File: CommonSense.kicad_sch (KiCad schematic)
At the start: 37 parts, among them J1 Conn_02x04_Counter_Clockwise, J2 Conn_01x02, J3 Conn_01x02, J5 Conn_ARM_SWD_TagConnect_TC203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, U1 NRF52810-QFAA-R7, U2 SHT41-AD1B-R2, Y1 ECS-.327-12.5-12R-TR, Y2 ABM11W-32.0000MHZ-7-D1X-T3

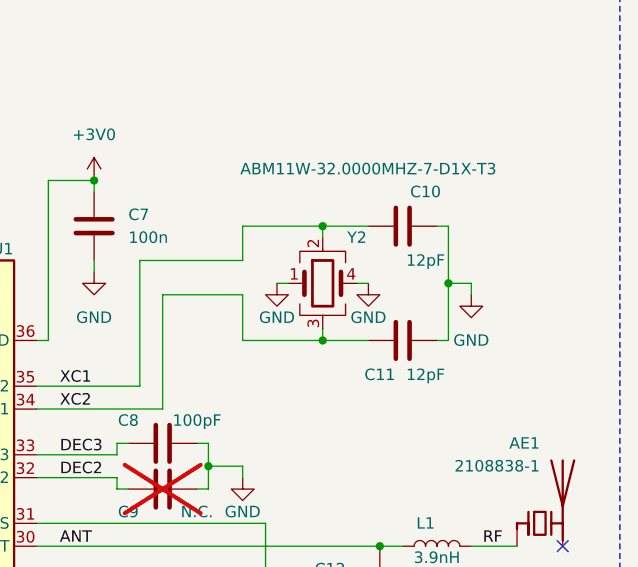
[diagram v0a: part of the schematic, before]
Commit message: Change crystal capacitor values
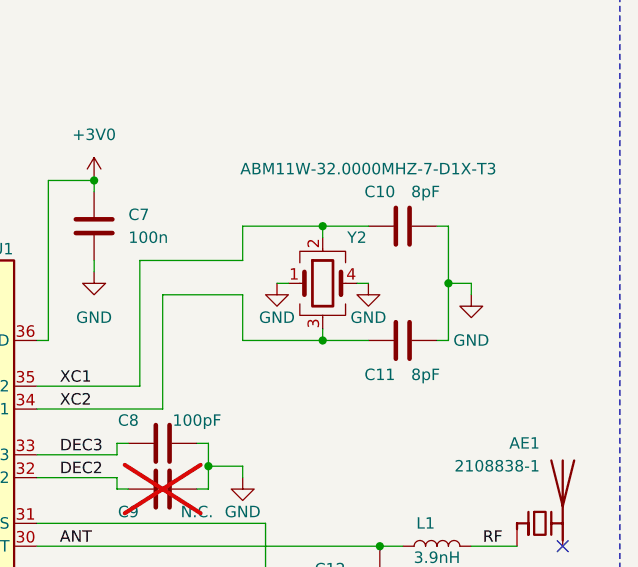
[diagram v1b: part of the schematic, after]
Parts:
- C10, C11: value 12pF -> 8pF
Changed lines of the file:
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@@
   (symbol (lib_id "Device:C") (at 251.46 66.04 90) (unit 1)
     (in_bom yes) (on_board yes) (dnp no)
-    (property "Reference" "C10" (at 254 62.23 90)
-      (effects (font (size 1.27 1.27)))
-    )
-    (property "Value" "12pF" (at 254 69.85 90)
+    (property "Reference" "C10" (at 248.92 62.23 90)
+      (effects (font (size 1.27 1.27)))
+    )
+    (property "Value" "8pF" (at 254 62.23 90)
       (effects (font (size 1.27 1.27)))
     )
@@
       (effects (font (size 1.27 1.27)))
     )
-    (property "Value" "12pF" (at 254 82.55 90)
-      (effects (font (size 1.27 1.27)))
-    )
+    (property "Value" "8pF" (at 254 82.55 90)
+      (effects (font (size 1.27 1.27)))
+    )

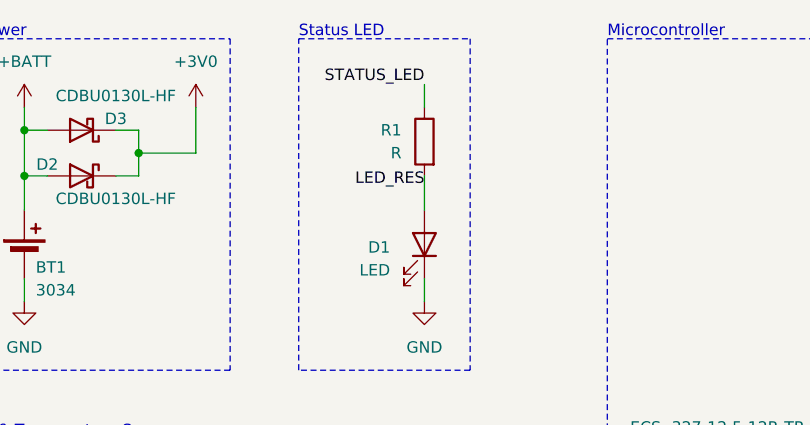
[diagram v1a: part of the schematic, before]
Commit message: Add 1k value to LED resistor
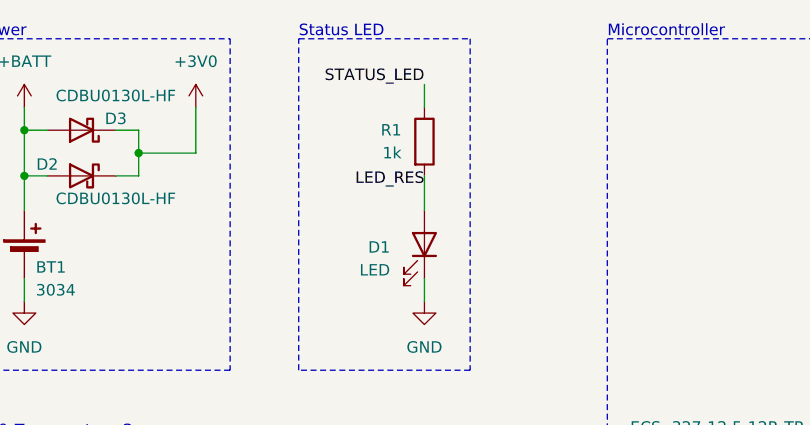
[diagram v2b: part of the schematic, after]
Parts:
- R1: value R -> 1k
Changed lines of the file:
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@@
     )
   )
-  (symbol (lib_id "Device:R") (at 72.39 44.45 0) (mirror y) (unit 1)
-    (in_bom yes) (on_board yes) (dnp no) (fields_autoplaced)
+  (symbol (lib_id "Device:R") (at 72.39 44.45 0) (unit 1)
+    (in_bom yes) (on_board yes) (dnp no)
     (property "Reference" "R1" (at 69.85 43.18 0)
-      (effects (font (size 1.27 1.27)) (justify left))
+      (effects (font (size 1.27 1.27)) (justify right))
     )
-    (property "Value" "R" (at 69.85 45.72 0)
-      (effects (font (size 1.27 1.27)) (justify left))
+    (property "Value" "1k" (at 69.85 45.72 0)
+      (effects (font (size 1.27 1.27)) (justify right))
     )
-    (property "Footprint" "Resistor_SMD:R_0603_1608Metric" (at 74.168 44.45 90)
+    (property "Footprint" "Resistor_SMD:R_0603_1608Metric" (at 70.612 44.45 90)
       (effects (font (size 1.27 1.27)) hide)
     )

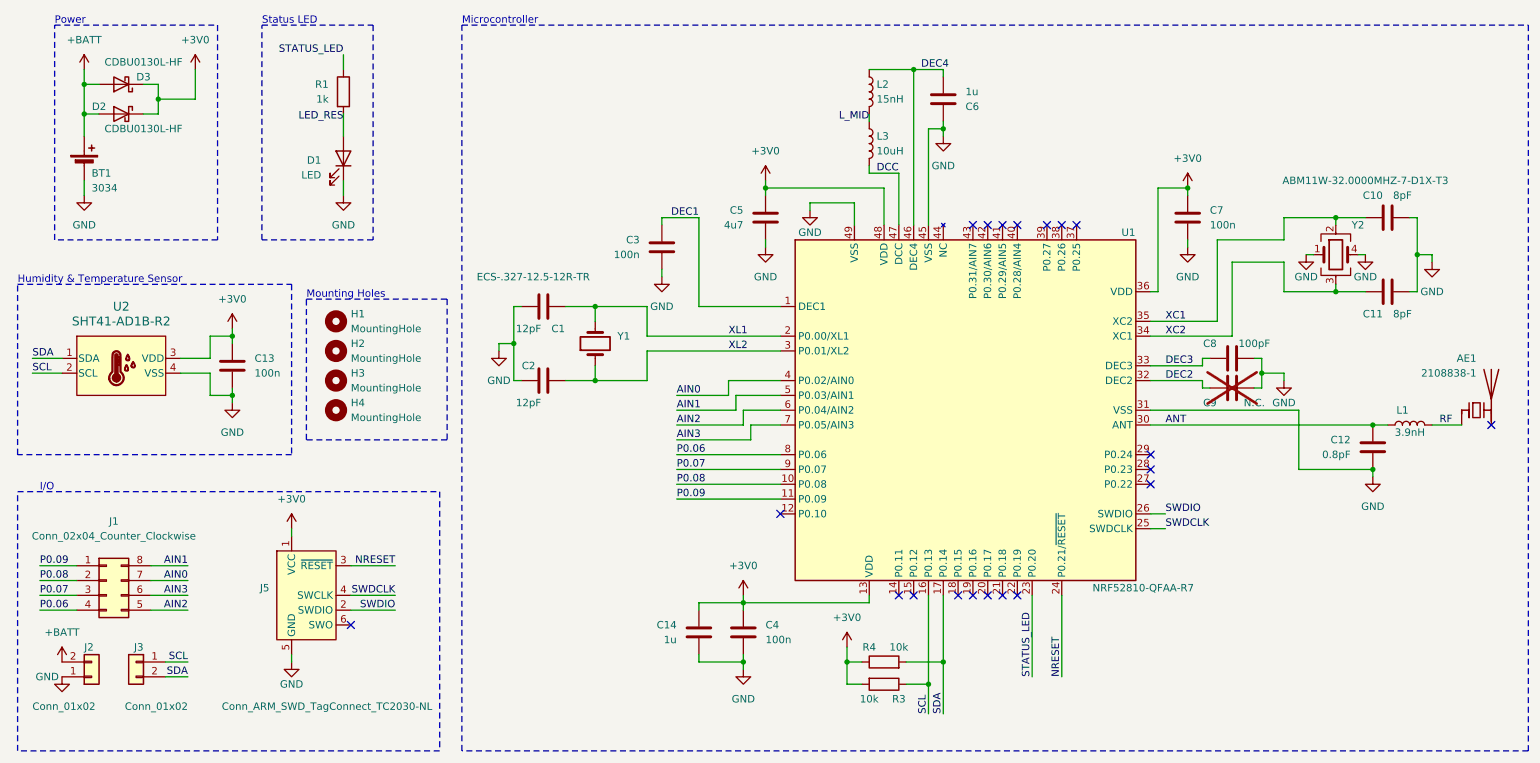
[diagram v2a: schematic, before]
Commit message: Fix component values
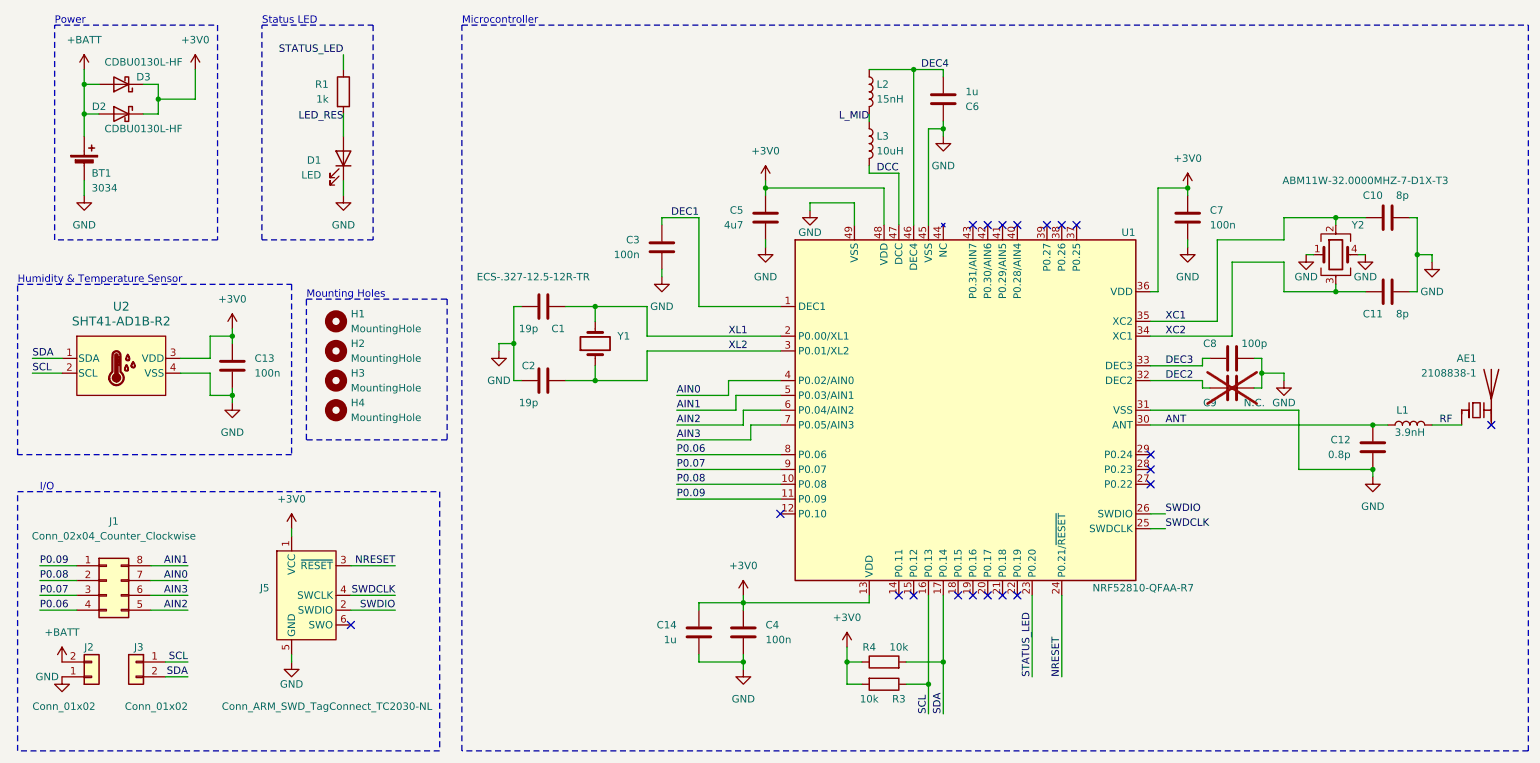
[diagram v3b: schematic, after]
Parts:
- C1, C2: value 12pF -> 19p
- C10, C11: value 8pF -> 8p
- C12: value 0.8pF -> 0.8p
- C8: value 100pF -> 100p
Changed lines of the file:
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@@
       (effects (font (size 1.27 1.27)))
     )
-    (property "Value" "12pF" (at 104.14 97.79 90)
+    (property "Value" "19p" (at 104.14 97.79 90)
       (effects (font (size 1.27 1.27)))
     )
@@
       (effects (font (size 1.27 1.27)))
     )
-    (property "Value" "100pF" (at 228.6 87.63 90)
+    (property "Value" "100p" (at 228.6 87.63 90)
       (effects (font (size 1.27 1.27)))
     )
@@
       (effects (font (size 1.27 1.27)) hide)
     )
-    (property "Datasheet" "~" (at 115.57 87.63 0)
+    (property "Datasheet" "https://www.mouser.de/datasheet/2/122/ECX-12R-1314062.pdf" (at 115.57 87.63 0)
       (effects (font (size 1.27 1.27)) hide)
     )
@@
       (effects (font (size 1.27 1.27)))
     )
-    (property "Value" "12pF" (at 104.14 85.09 90)
+    (property "Value" "19p" (at 104.14 85.09 90)
       (effects (font (size 1.27 1.27)))
     )
@@
       (effects (font (size 1.27 1.27)))
     )
-    (property "Value" "8pF" (at 254 62.23 90)
+    (property "Value" "8p" (at 254 62.23 90)
       (effects (font (size 1.27 1.27)))
     )
@@
       (effects (font (size 1.27 1.27)) (justify right))
     )
-    (property "Value" "0.8pF" (at 245.11 106.68 0)
+    (property "Value" "0.8p" (at 245.11 106.68 0)
       (effects (font (size 1.27 1.27)) (justify right))
     )
@@
       (effects (font (size 1.27 1.27)))
     )
-    (property "Value" "8pF" (at 254 82.55 90)
-      (effects (font (size 1.27 1.27)))
-    )
+    (property "Value" "8p" (at 254 82.55 90)
+      (effects (font (size 1.27 1.27)))
+    )
